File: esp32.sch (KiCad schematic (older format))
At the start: 9 parts, among them U3 ESP32-WROOM

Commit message: Add: Improved layout
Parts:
- added SW1, SW2: SW_Push, Button_Switch_SMD:SW_SPST_EVQP7A, symbol Switch:SW_Push
- C6: footprint Capacitor_SMD:C_0805_2012Metric -> Capacitor_SMD:C_0603_1608Metric
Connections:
- net GND: now also SW1.2, SW2.2
- net at U3.10 (IO25): now also D4.1 (K)
- net BUT_B: now reaches U3.30 (IO18)
- net BUT_B: now also SW1.1
- net BUT_A: now reaches U3.31 (IO19)
- net BUT_A: now also SW2.1
- net at U3.6 (IO34): no longer D4.1 (K)
- no-connect marks 25 -> 23
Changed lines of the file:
@@
 Comment4 ""
 $EndDescr
-$Comp
-L ESP32-footprints-Shem-Lib:ESP32-WROOM U3
-U 1 1 5EB13525
-P 5600 4000
-F 0 "U3" H 5575 5387 60  0000 C CNN
-F 1 "ESP32-WROOM" H 5575 5281 60  0000 C CNN
-F 2 "RF_Module:ESP32-WROOM-32" H 5950 5350 60  0001 C CNN
-F 3 "" H 5150 4450 60  0001 C CNN
-	1    5600 4000
-	1    0    0    -1
-$EndComp
 Text HLabel 4000 3500 0    49   Input ~ 0
 MCU_ENABLE
@@
 	7750 3650 6500 3650
 Connection ~ 7750 3650
-NoConn ~ 6500 3850
-NoConn ~ 6500 3950
 NoConn ~ 6500 4150
 NoConn ~ 6500 3250
@@
 NoConn ~ 5250 5050
 NoConn ~ 4650 4600
-NoConn ~ 4650 4500
 NoConn ~ 4650 4400
-NoConn ~ 4650 4300
-NoConn ~ 4650 4200
 NoConn ~ 4650 4100
 NoConn ~ 4650 4000
@@
 F 0 "C6" V 4415 3196 50  0000 L CNN
 F 1 "0.1uF/25V" V 4500 3100 50  0000 L CNN
-F 2 "Capacitor_SMD:C_0805_2012Metric" H 4338 3000 50  0001 C CNN
+F 2 "Capacitor_SMD:C_0603_1608Metric" H 4338 3000 50  0001 C CNN
 F 3 "~" H 4300 3150 50  0001 C CNN
 F 4 "Mouser" H 4300 3150 50  0001 C CNN "Vendor"
@@
 	4300 3500 4300 3750
 Wire Wire Line
-	4500 4000 4500 3800
-Wire Wire Line
-	4500 3800 4650 3800
-Wire Wire Line
 	4100 4000 4500 4000
+$Comp
+L Switch:SW_Push SW2
+U 1 1 5EA157F9
+P 6950 5550
+F 0 "SW2" H 6950 5835 50  0000 C CNN
+F 1 "SW_Push" H 6950 5744 50  0000 C CNN
+F 2 "Button_Switch_SMD:SW_SPST_EVQP7A" H 6950 5750 50  0001 C CNN
+F 3 "~" H 6950 5750 50  0001 C CNN
+	1    6950 5550
+	1    0    0    -1
+$EndComp
+NoConn ~ 4650 4500
+$Comp
+L ESP32-footprints-Shem-Lib:ESP32-WROOM U3
+U 1 1 5EB13525
+P 5600 4000
+F 0 "U3" H 5575 5387 60  0000 C CNN
+F 1 "ESP32-WROOM" H 5575 5281 60  0000 C CNN
+F 2 "RF_Module:ESP32-WROOM-32" H 5950 5350 60  0001 C CNN
+F 3 "" H 5150 4450 60  0001 C CNN
+	1    5600 4000
+	1    0    0    -1
+$EndComp
+NoConn ~ 4650 4300
+Wire Wire Line
+	6550 5550 6750 5550
+Text Label 6550 5700 3    50   ~ 0
+BUT_A
+Wire Wire Line
+	6550 5700 6550 5550
+Text Label 7500 5700 3    50   ~ 0
+BUT_B
+Wire Wire Line
+	7500 5700 7500 5550
+Wire Wire Line
+	7500 5550 7700 5550
+$Comp
+L power:GND #PWR0167
+U 1 1 5EA30277
+P 8100 5650
+F 0 "#PWR0167" H 8100 5400 50  0001 C CNN
+F 1 "GND" H 8105 5477 50  0000 C CNN
+F 2 "" H 8100 5650 50  0001 C CNN
+F 3 "" H 8100 5650 50  0001 C CNN
+	1    8100 5650
+	1    0    0    -1
+$EndComp
+Wire Wire Line
+	8100 5650 8100 5550
+$Comp
+L power:GND #PWR0168
+U 1 1 5EA30DBD
+P 7150 5650
+F 0 "#PWR0168" H 7150 5400 50  0001 C CNN
+F 1 "GND" H 7155 5477 50  0000 C CNN
+F 2 "" H 7150 5650 50  0001 C CNN
+F 3 "" H 7150 5650 50  0001 C CNN
+	1    7150 5650
+	1    0    0    -1
+$EndComp
+Wire Wire Line
+	7150 5650 7150 5550
+Text Label 6600 3850 0    50   ~ 0
+BUT_A
+Wire Wire Line
+	6600 3850 6500 3850
+Text Label 6600 3950 0    50   ~ 0
+BUT_B
+Wire Wire Line
+	6600 3950 6500 3950
+NoConn ~ 4650 3800
+Wire Wire Line
+	4500 4000 4500 4200
+Wire Wire Line
+	4500 4200 4650 4200
+$Comp
+L Switch:SW_Push SW1
+U 1 1 5E92AD3D
+P 7900 5550
+F 0 "SW1" H 7900 5835 50  0000 C CNN
+F 1 "SW_Push" H 7900 5744 50  0000 C CNN
+F 2 "Button_Switch_SMD:SW_SPST_EVQP7A" H 7900 5750 50  0001 C CNN
+F 3 "~" H 7900 5750 50  0001 C CNN
+	1    7900 5550
+	1    0    0    -1
+$EndComp
 $EndSCHEMATC

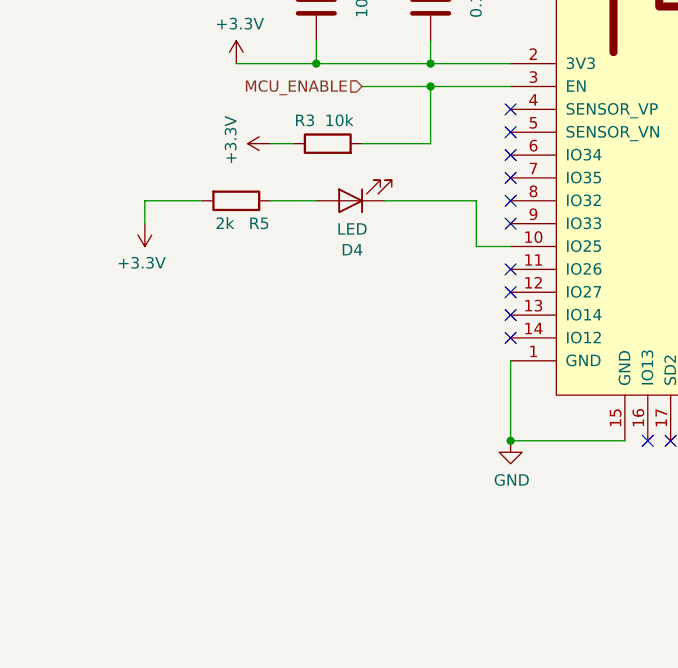
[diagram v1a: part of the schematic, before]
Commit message: Add: Watch crystal, switches
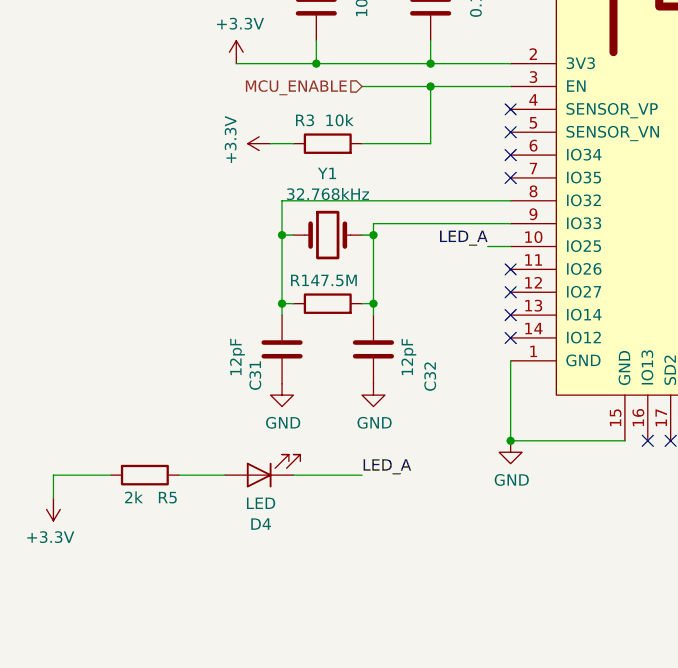
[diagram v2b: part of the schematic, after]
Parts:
- added C31, C32: 12pF, Capacitor_SMD:C_0603_1608Metric, symbol Device:C
- added R14: 7.5M, Resistor_SMD:R_0603_1608Metric, symbol Device:R
- added Y1: 32.768kHz, Crystal:Crystal_SMD_MicroCrystal_CC7V-T1A-2Pin_3.2x1.5mm, symbol Device:Crystal
- SW1, SW2: Vendor (none) -> Digi-Key; Vendor Price 100p (none) -> 0.20; Vendor Price 10p (none) -> 0.21; Vendor Price 1p (none) -> 0.23; Vendor SKU (none) -> P16763CT-ND
- U3: Vendor (none) -> Digi-Key; Vendor Price 1p (none) -> 2.90; Vendor SKU (none) -> 1904-1023-1-ND
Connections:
- net GND: now also C31.1, C32.1
- net LED_A: now reaches D4.1 (K), U3.10 (IO25)
- net at U3.8 (IO32): now also C31.2, R14.1, Y1.1
- net at U3.9 (IO33): now also C32.2, R14.2, Y1.2
- no-connect marks 23 -> 21
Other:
- moved on the sheet: D4, R5
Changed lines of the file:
@@
 NoConn ~ 4650 4600
 NoConn ~ 4650 4400
-NoConn ~ 4650 4100
-NoConn ~ 4650 4000
 NoConn ~ 4650 3900
 Wire Wire Line
@@
 $EndComp
 $Comp
-L Device:LED D4
-U 1 1 5EF1FB24
-P 3950 4000
-F 0 "D4" H 3943 4216 50  0000 C CNN
-F 1 "LED" H 3943 4125 50  0000 C CNN
-F 2 "LED_SMD:LED_0805_2012Metric" H 3950 4000 50  0001 C CNN
-F 3 "~" H 3950 4000 50  0001 C CNN
-	1    3950 4000
-	-1   0    0    1
-$EndComp
-Wire Wire Line
-	3800 4000 3600 4000
-$Comp
-L Device:R R?
-U 1 1 5EF1FB2C
-P 3450 4000
-AR Path="/5EF1FB2C" Ref="R?"  Part="1"
-AR Path="/5EA0B24D/5EF1FB2C" Ref="R?"  Part="1"
-AR Path="/5EB11343/5EF1FB2C" Ref="R5"  Part="1"
-F 0 "R5" V 3550 4100 50  0000 C CNN
-F 1 "2k" V 3550 3950 50  0000 C CNN
-F 2 "Resistor_SMD:R_0603_1608Metric" V 3335 4000 50  0001 C CNN
-F 3 "~" H 3450 4000 50  0001 C CNN
-	1    3450 4000
-	0    1    1    0
-$EndComp
-Wire Wire Line
-	3050 4000 3050 4100
-$Comp
-L power:+3.3V #PWR0119
-U 1 1 5EF1FB33
-P 3050 4100
-F 0 "#PWR0119" H 3050 3950 50  0001 C CNN
-F 1 "+3.3V" H 3065 4273 50  0000 C CNN
-F 2 "" H 3050 4100 50  0001 C CNN
-F 3 "" H 3050 4100 50  0001 C CNN
-	1    3050 4100
-	-1   0    0    1
-$EndComp
-Wire Wire Line
-	3050 4000 3300 4000
-$Comp
 L Device:R R?
 U 1 1 5EB7EC19
@@
 Wire Wire Line
 	4300 3500 4300 3750
-Wire Wire Line
-	4100 4000 4500 4000
 $Comp
 L Switch:SW_Push SW2
@@
 F 2 "Button_Switch_SMD:SW_SPST_EVQP7A" H 6950 5750 50  0001 C CNN
 F 3 "~" H 6950 5750 50  0001 C CNN
+F 4 "Digi-Key" H 6950 5550 50  0001 C CNN "Vendor"
+F 5 "0.20" H 6950 5550 50  0001 C CNN "Vendor Price 100p"
+F 6 "0.21" H 6950 5550 50  0001 C CNN "Vendor Price 10p"
+F 7 "0.23" H 6950 5550 50  0001 C CNN "Vendor Price 1p"
+F 8 "P16763CT-ND " H 6950 5550 50  0001 C CNN "Vendor SKU"
 	1    6950 5550
 	1    0    0    -1
@@
 F 1 "ESP32-WROOM" H 5575 5281 60  0000 C CNN
 F 2 "RF_Module:ESP32-WROOM-32" H 5950 5350 60  0001 C CNN
-F 3 "" H 5150 4450 60  0001 C CNN
+F 3 "https://www.espressif.com/sites/default/files/documentation/esp32-wroom-32d_esp32-wroom-32u_datasheet_en.pdf" H 5150 4450 60  0001 C CNN
+F 4 "Digi-Key" H 5600 4000 50  0001 C CNN "Vendor"
+F 5 "2.90" H 5600 4000 50  0001 C CNN "Vendor Price 1p"
+F 6 "1904-1023-1-ND " H 5600 4000 50  0001 C CNN "Vendor SKU"
 	1    5600 4000
 	1    0    0    -1
@@
 	6600 3950 6500 3950
 NoConn ~ 4650 3800
-Wire Wire Line
-	4500 4000 4500 4200
-Wire Wire Line
-	4500 4200 4650 4200
 $Comp
 L Switch:SW_Push SW1
@@
 F 2 "Button_Switch_SMD:SW_SPST_EVQP7A" H 7900 5750 50  0001 C CNN
 F 3 "~" H 7900 5750 50  0001 C CNN
+F 4 "Digi-Key" H 7900 5550 50  0001 C CNN "Vendor"
+F 5 "0.20" H 7900 5550 50  0001 C CNN "Vendor Price 100p"
+F 6 "0.21" H 7900 5550 50  0001 C CNN "Vendor Price 10p"
+F 7 "0.23" H 7900 5550 50  0001 C CNN "Vendor Price 1p"
+F 8 "P16763CT-ND " H 7900 5550 50  0001 C CNN "Vendor SKU"
 	1    7900 5550
 	1    0    0    -1
 $EndComp
+Wire Wire Line
+	4650 4200 4550 4200
+$Comp
+L Device:Crystal Y1
+U 1 1 5E546ED8
+P 3850 4150
+F 0 "Y1" H 3850 4418 50  0000 C CNN
+F 1 "32.768kHz" H 3850 4327 50  0000 C CNN
+F 2 "Crystal:Crystal_SMD_MicroCrystal_CC7V-T1A-2Pin_3.2x1.5mm" H 3850 4150 50  0001 C CNN
+F 3 "https://docs.rs-online.com/3f68/0900766b80d2cb67.pdf" H 3850 4150 50  0001 C CNN
+F 4 "RS Online" H 3850 4150 50  0001 C CNN "Vendor"
+F 5 "0.77" H 3850 4150 50  0001 C CNN "Vendor Price 100p"
+F 6 "0.84" H 3850 4150 50  0001 C CNN "Vendor Price 10p"
+F 7 "1.05" H 3850 4150 50  0001 C CNN "Vendor Price 1p"
+F 8 "672-7638" H 3850 4150 50  0001 C CNN "Vendor SKU"
+	1    3850 4150
+	1    0    0    -1
+$EndComp
+$Comp
+L Device:C C?
+U 1 1 5E548892
+P 3650 4650
+AR Path="/5EA5FEAD/5E548892" Ref="C?"  Part="1"
+AR Path="/5EB11343/5E548892" Ref="C31"  Part="1"
+F 0 "C31" V 3765 4696 50  0000 L CNN
+F 1 "12pF" V 3850 4600 50  0000 L CNN
+F 2 "Capacitor_SMD:C_0603_1608Metric" H 3688 4500 50  0001 C CNN
+F 3 "~" H 3650 4650 50  0001 C CNN
+F 4 "" H 3650 4650 50  0001 C CNN "Vendor"
+F 5 "" H 3650 4650 50  0001 C CNN "Vendor Price 10p"
+F 6 "" H 3650 4650 50  0001 C CNN "Vendor Price 1p"
+F 7 "" H 3650 4650 50  0001 C CNN "Vendor SKU"
+	1    3650 4650
+	-1   0    0    1
+$EndComp
+$Comp
+L Device:C C?
+U 1 1 5E54B6BD
+P 4050 4650
+AR Path="/5EA5FEAD/5E54B6BD" Ref="C?"  Part="1"
+AR Path="/5EB11343/5E54B6BD" Ref="C32"  Part="1"
+F 0 "C32" V 3800 4700 50  0000 L CNN
+F 1 "12pF" V 3900 4600 50  0000 L CNN
+F 2 "Capacitor_SMD:C_0603_1608Metric" H 4088 4500 50  0001 C CNN
+F 3 "~" H 4050 4650 50  0001 C CNN
+F 4 "" H 4050 4650 50  0001 C CNN "Vendor"
+F 5 "" H 4050 4650 50  0001 C CNN "Vendor Price 10p"
+F 6 "" H 4050 4650 50  0001 C CNN "Vendor Price 1p"
+F 7 "" H 4050 4650 50  0001 C CNN "Vendor SKU"
+	1    4050 4650
+	-1   0    0    1
+$EndComp
+Wire Wire Line
+	4650 4000 3650 4000
+Wire Wire Line
+	3650 4000 3650 4150
+Wire Wire Line
+	3650 4150 3700 4150
+Wire Wire Line
+	4000 4150 4050 4150
+Wire Wire Line
+	4050 4150 4050 4100
+Wire Wire Line
+	4050 4100 4650 4100
+Wire Wire Line
+	2650 5200 2900 5200
+$Comp
+L power:+3.3V #PWR0119
+U 1 1 5EF1FB33
+P 2650 5300
+F 0 "#PWR0119" H 2650 5150 50  0001 C CNN
+F 1 "+3.3V" H 2665 5473 50  0000 C CNN
+F 2 "" H 2650 5300 50  0001 C CNN
+F 3 "" H 2650 5300 50  0001 C CNN
+	1    2650 5300
+	-1   0    0    1
+$EndComp
+Wire Wire Line
+	2650 5200 2650 5300
+$Comp
+L Device:R R?
+U 1 1 5EF1FB2C
+P 3050 5200
+AR Path="/5EF1FB2C" Ref="R?"  Part="1"
+AR Path="/5EA0B24D/5EF1FB2C" Ref="R?"  Part="1"
+AR Path="/5EB11343/5EF1FB2C" Ref="R5"  Part="1"
+F 0 "R5" V 3150 5300 50  0000 C CNN
+F 1 "2k" V 3150 5150 50  0000 C CNN
+F 2 "Resistor_SMD:R_0603_1608Metric" V 2935 5200 50  0001 C CNN
+F 3 "~" H 3050 5200 50  0001 C CNN
+	1    3050 5200
+	0    1    1    0
+$EndComp
+Wire Wire Line
+	3400 5200 3200 5200
+$Comp
+L Device:LED D4
+U 1 1 5EF1FB24
+P 3550 5200
+F 0 "D4" H 3543 5416 50  0000 C CNN
+F 1 "LED" H 3543 5325 50  0000 C CNN
+F 2 "LED_SMD:LED_0805_2012Metric" H 3550 5200 50  0001 C CNN
+F 3 "~" H 3550 5200 50  0001 C CNN
+	1    3550 5200
+	-1   0    0    1
+$EndComp
+Text Label 4000 5200 0    50   ~ 0
+LED_A
+Wire Wire Line
+	4000 5200 3700 5200
+Text Label 4550 4200 2    50   ~ 0
+LED_A
+$Comp
+L power:GND #PWR0166
+U 1 1 5E56ACD9
+P 4050 4800
+F 0 "#PWR0166" H 4050 4550 50  0001 C CNN
+F 1 "GND" H 4055 4627 50  0000 C CNN
+F 2 "" H 4050 4800 50  0001 C CNN
+F 3 "" H 4050 4800 50  0001 C CNN
+	1    4050 4800
+	1    0    0    -1
+$EndComp
+$Comp
+L power:GND #PWR0169
+U 1 1 5E56BBE5
+P 3650 4800
+F 0 "#PWR0169" H 3650 4550 50  0001 C CNN
+F 1 "GND" H 3655 4627 50  0000 C CNN
+F 2 "" H 3650 4800 50  0001 C CNN
+F 3 "" H 3650 4800 50  0001 C CNN
+	1    3650 4800
+	1    0    0    -1
+$EndComp
+Wire Wire Line
+	4050 4150 4050 4450
+Connection ~ 4050 4150
+Wire Wire Line
+	3650 4150 3650 4450
+Connection ~ 3650 4150
+$Comp
+L Device:R R?
+U 1 1 5E5AEEB4
+P 3850 4450
+AR Path="/5E5AEEB4" Ref="R?"  Part="1"
+AR Path="/5EA0B24D/5E5AEEB4" Ref="R?"  Part="1"
+AR Path="/5EB11343/5E5AEEB4" Ref="R14"  Part="1"
+F 0 "R14" V 3950 4550 50  0000 C CNN
+F 1 "7.5M" V 3950 4400 50  0000 C CNN
+F 2 "Resistor_SMD:R_0603_1608Metric" V 3735 4450 50  0001 C CNN
+F 3 "~" H 3850 4450 50  0001 C CNN
+	1    3850 4450
+	0    -1   -1   0
+$EndComp
+Wire Wire Line
+	4000 4450 4050 4450
+Connection ~ 4050 4450
+Wire Wire Line
+	4050 4450 4050 4500
+Wire Wire Line
+	3700 4450 3650 4450
+Connection ~ 3650 4450
+Wire Wire Line
+	3650 4450 3650 4500
 $EndSCHEMATC
